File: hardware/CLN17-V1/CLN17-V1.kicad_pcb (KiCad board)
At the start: 4 copper layers, 38 x 38 mm, 92 parts, among them IC1 STM32G431CB, J1 Motor, J2 USB_C, J3 CTRL, J4 PWR, J5 CAN, J6 CAN, J7 IO, SW1 SW_Push, SW2 SW_Push, U1 TMC2209, U2 TLE5012B, U4 XC6206, U5 USBLC6-4SC6, U6 USBLC6-4SC6, U7 USBLC6-4SC6, U8 TJA1051, U9 TP6841, Y1 8M

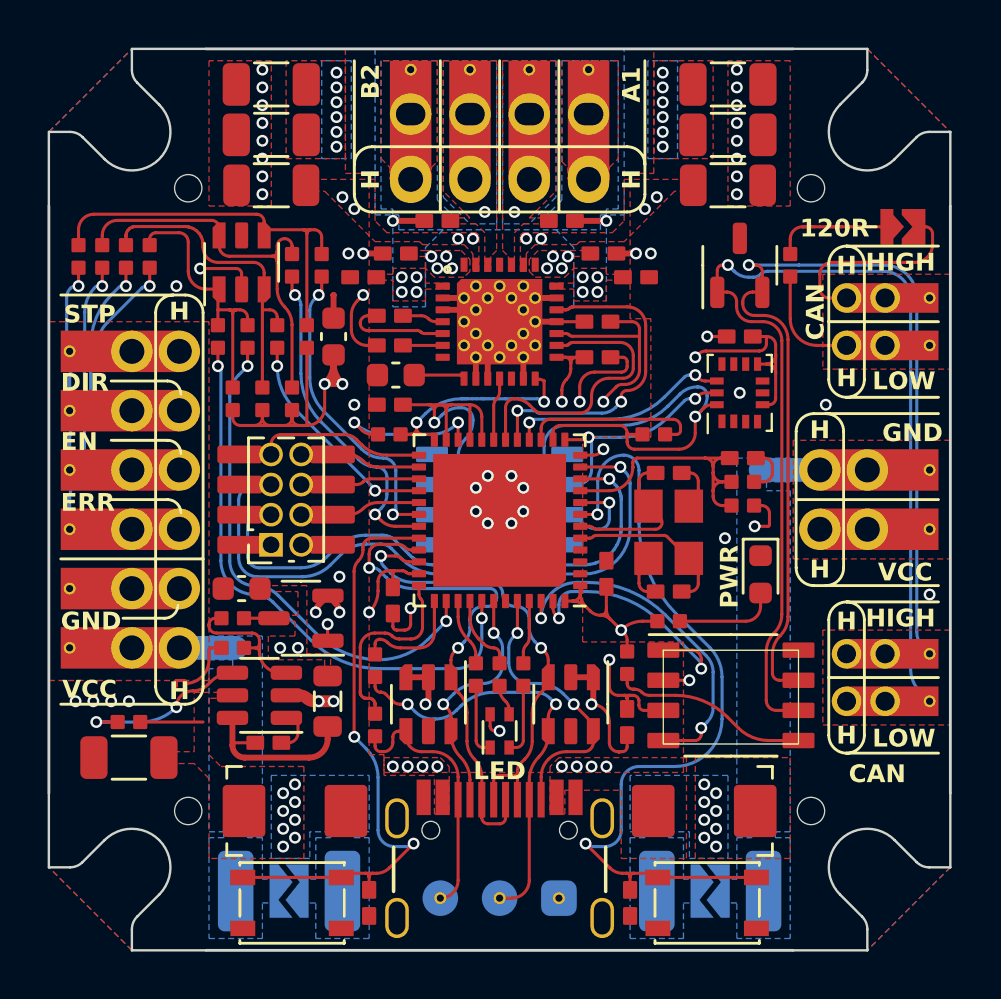
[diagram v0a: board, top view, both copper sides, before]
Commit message: V1.1 fixes
- Optimised circuit power supply:
	- Improved power polygon layout;
	- Improved DCDC converter layout
- Improved Type-C compatibility:
	- Added full-featured UCPD interface;
	- Added 5.1k resistors in case UCPD doesn't work
- Optimised components:
	- ESD protection reduced form factor;
	- Correct USB Type-C connector with both CC lines
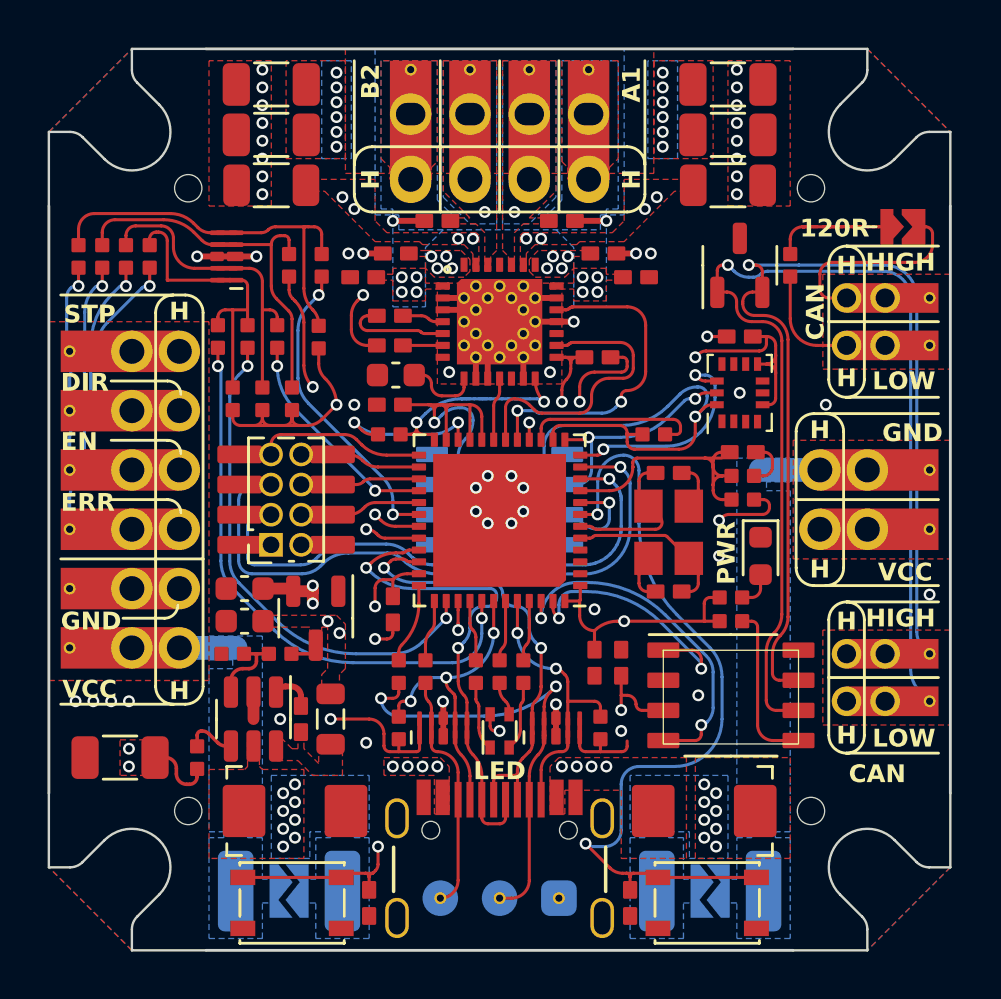
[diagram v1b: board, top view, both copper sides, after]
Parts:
- removed C27: 100n, FP_lib:C0402
- removed U7: USBLC6-4SC6, FP_lib:SOT-23-6
- added R32: 5.1k, FP_lib:R0402, F.Cu at (29.8, 43.6)
- added R8: 5.1k, FP_lib:R0402, F.Cu at (38.2, 43.6)
- added U3: H5VU25U, FP_lib:DFN-2510, F.Cu at (22.5, 23.8)
- R1, R16, R17, R18, R19, R2, R23, R26, R28, R3, R4: value 100 -> 120
- U5, U6: value USBLC6-4SC6 -> H5VU25U; footprint FP_lib:SOT-23-6 -> FP_lib:DFN-2510
- moved U5 21.4 mm to (31.6, 43.6)
- moved C26 11.3 mm to (23.2, 37.8), turned to 180 degrees
- moved U6 5.47 mm to (36.4, 43.6), turned to 90 degrees
- moved R25 4.71 mm to (43.8, 39.1), turned to 180 degrees
- moved C4 3.78 mm to (38.0, 40.9), turned to -90 degrees
- moved R7 3.24 mm to (21.2, 44.9), turned to -90 degrees
- moved R30 2.81 mm to (43.8, 38.1)
- moved C1 2.51 mm to (39.1, 40.9), turned to 90 degrees
- moved R9 2.50 mm to (24.8, 40.5)
- moved R4 2.46 mm to (29.8, 41.2)
- moved R23 2.14 mm to (30.9, 41.2)
- moved C25 1.70 mm to (25.6, 43.2), turned to 90 degrees
- moved C24 1.38 mm to (23.2, 39.1)
- moved U9 1.03 mm to (23.6, 43.2), turned to -90 degrees
- moved D3 0.77 mm to (45.0, 36.4)
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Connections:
- IC1 pad 12: /VREF -> /CS_IMU
- IC1 pad 16: /CS_IMU -> /_DIR/SCL
- IC1 pad 31: /_DIR/SCL -> /PD_CC1
- IC1 pad 32: /SW1 -> /PD_CC2
- IC1 pad 39: /RED -> /SW1
- IC1 pad 40: /BLUE -> /RED
- IC1 pad 42: /PD_CC1 -> /PD_CC2
- IC1 pad 43: unconnected-(IC1-PB5-Pad43) -> /BLUE
- IC1 pad 44: /PD_CC2 -> /PD_CC1
- J2 pad A5: /PD_CC1 -> /PD_CC2
- J2 pad A8: /SWCLK -> /SWDIO
- J2 pad B5: /PD_CC2 -> /PD_CC1
- J2 pad B8: /SWDIO -> /SWCLK
- U1 pad 17: /VREF -> unconnected-(U1-VREF-Pad17)
- U5 pad 1: /ERR/UART -> GND
- U5 pad 2: GND -> /SWCLK
- U5 pad 3: /EN -> GND
- U5 pad 4: /STEP/SDA -> /PD_CC2
- U5 pad 5: unconnected-(U5-VBUS-Pad5) -> /USB_DN
- U5 pad 6: /DIR/SCL -> /USB_DN
- U6 pad 1: /USB_DN -> /USB_DP
- U6 pad 2: GND -> /SWDIO
- U6 pad 4: /SWDIO -> /PD_CC1
- U6 pad 5: unconnected-(U6-VBUS-Pad5) -> GND
- U6 pad 6: /PD_CC1 -> GND
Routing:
- net /VREF: track 11.9 -> 0.00 mm, vias 2 -> 0
- net /PD_CC1: track 10.3 -> 22.0 mm, vias 2 -> 3
- net /PD_CC2: track 12.0 -> 22.6 mm, vias 2 -> 4
- net /SWCLK: track 18.4 -> 10.1 mm, vias 2 -> 0
- net /SWDIO: track 11.4 -> 19.5 mm, vias 0 -> 2
- net /LX: track 7.59 -> 0.00 mm
- net /SW1: track 25.6 -> 20.3 mm, vias 2 -> 3
- net Net-(U9-EN): track 7.37 -> 2.21 mm, vias 2 -> 0
- net /_SWDIO: track 8.27 -> 3.49 mm
- net +3V3: track 61.0 -> 57.5 mm, vias 10 -> 9
- net Net-(U9-FB): track 6.22 -> 3.36 mm
- net Net-(D3-A): track 4.29 -> 1.56 mm
- net GND: track 47.4 -> 45.1 mm, vias 51 -> 54
- net /_SWCLK: track 4.82 -> 2.59 mm
- net VBUS: track 7.92 -> 9.51 mm, vias 38 -> 40
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- added copper zone on F.Cu, net /LX
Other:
- board text added: ".V1.1"
- board text added: "GD"
- board text removed: ".V1"
- board text removed: "G"
